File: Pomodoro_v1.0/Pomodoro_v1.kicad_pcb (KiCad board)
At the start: 2 copper layers, 70 x 50 mm, 88 parts, among them J1 BATT, J13 SWIM, J2 NTC, J3 USB_OTG, J5 UART, M1 MOUNTING-HOLE, M2 MOUNTING-HOLE, M3 MOUNTING-HOLE, M4 MOUNTING-HOLE, Q1 BC807, Q2 BC807, SW1 SLIDER, SW2 BUTTON_SPST, U1 MCP73833, U2 TPS62260, U3 STM8L151C2T6, U4 AS1122

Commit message: update footprints with 3D models
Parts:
- SW1: footprint SLIDE_SWITCHES: 5MS1S102AM6QE -> SLIDE_SWITCHES:5MS1S102AM6QE
- SW2: footprint NINIGI TACTS-24N-F:NINIGI TACTS-24N-F -> NINIGI_TACTS-24N-F:NINIGI_TACTS-24N-F
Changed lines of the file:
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@@
-(kicad_pcb (version 4) (host pcbnew 4.0.7-e2-6376~58~ubuntu16.04.1)
+(kicad_pcb (version 4) (host pcbnew 4.0.7)
   (general
     (links 166)
@@
     (pad_to_mask_clearance 0.2)
     (aux_axis_origin 0 0)
-    (visible_elements FFFEF77F)
+    (visible_elements 7FFFF7FF)
     (pcbplotparams
       (layerselection 0x00030_80000001)
@@
     (add_net VCC)
   )
-  (module BUZZERS_TDK:BUZZERS_TDK (layer F.Cu)
-    (at 60 102)
-    (fp_text reference BZ1 (at 0.254 -7.366) (layer F.SilkS)
-      (effects (font (size 1 1) (thickness 0.15)))
-    )
-    (fp_text value Buzzer (at 0 -2.286) (layer F.Fab)
-      (effects (font (size 1 1) (thickness 0.15)))
-    )
-    (fp_circle (center 0 0) (end 6.604 0) (layer F.SilkS) (width 0.15))
-    (pad 1 thru_hole circle (at 2.5 0) (size 2 2) (drill 0.8) (layers *.Cu *.Mask)
-      (net 1 VCC))
-    (pad 2 thru_hole circle (at -2.5 0) (size 2 2) (drill 0.8) (layers *.Cu *.Mask)
-      (net 2 /BUZZER))
-    (pad "" np_thru_hole circle (at 0 -4.5) (size 0.8 0.8) (drill 0.8) (layers *.Cu *.Mask))
-    (pad "" np_thru_hole circle (at 0 4.5) (size 0.8 0.8) (drill 0.8) (layers *.Cu *.Mask))
-  )
   (module Capacitors_SMD:C_0805 (layer F.Cu)
     (at 211.465001 119.155)
@@
     (pad 6 smd rect (at -2.9 0.35 270) (size 1.2 1.9) (layers F.Cu F.Mask)
       (net 4 GND))
-    (model ${KISYS3DMOD}/Connectors_USB.3dshapes/USB_Micro-B_Molex-105017-0001.wrl
+    (model ${KISYS3DMOD}/Connectors_USB.3dshapes/MOLEX_1050170001.wrl
       (at (xyz 0 0 0))
       (scale (xyz 1 1 1))
@@
     )
   )
-  (module "SLIDE_SWITCHES: 5MS1S102AM6QE" (layer F.Cu)
-    (at 40 79 270)
-    (fp_text reference SW1 (at -8.5 6 360) (layer F.SilkS)
-      (effects (font (size 1 1) (thickness 0.15)))
-    )
-    (fp_text value SLIDER (at -0.5 4 270) (layer F.Fab)
-      (effects (font (size 1 1) (thickness 0.15)))
-    )
-    (fp_line (start -0.5 11.5) (end -0.5 16) (layer F.SilkS) (width 0.15))
-    (fp_line (start -0.5 16) (end 3.5 16) (layer F.SilkS) (width 0.15))
-    (fp_line (start 3.5 16) (end 3.5 11.5) (layer F.SilkS) (width 0.15))
-    (fp_line (start 7.5 8) (end 7.5 2.5) (layer F.SilkS) (width 0.15))
-    (fp_line (start 7.5 2.5) (end -7.5 2.5) (layer F.SilkS) (width 0.15))
-    (fp_line (start -7.5 2.5) (end -7.5 8) (layer F.SilkS) (width 0.15))
-    (fp_line (start -7 11.5) (end 7.5 11.5) (layer F.SilkS) (width 0.15))
-    (pad 1 thru_hole circle (at 4.699 -0.127 270) (size 3 3) (drill 1.85) (layers *.Cu *.Mask)
-      (net 60 "Net-(SW1-Pad1)"))
-    (pad 2 thru_hole circle (at 0 0 270) (size 3 3) (drill 1.85) (layers *.Cu *.Mask)
-      (net 23 +BATT))
-    (pad 3 thru_hole circle (at -4.699 -0.127 270) (size 3 3) (drill 1.85) (layers *.Cu *.Mask)
-      (net 3 +4V))
-    (pad "" thru_hole circle (at 6.604 9.525 270) (size 3 3) (drill 1.85) (layers *.Cu *.Mask))
-    (pad "" thru_hole circle (at -6.604 9.525 270) (size 3 3) (drill 1.85) (layers *.Cu *.Mask))
-  )
-  (module "NINIGI TACTS-24N-F:NINIGI TACTS-24N-F" (layer F.Cu)
-    (at 39 99)
-    (fp_text reference SW2 (at 2 9.5) (layer F.SilkS)
-      (effects (font (size 1 1) (thickness 0.15)))
-    )
-    (fp_text value BUTTON_SPST (at 7 -4.5) (layer F.Fab)
-      (effects (font (size 1 1) (thickness 0.15)))
-    )
-    (fp_line (start 0 -1) (end 0 -3.5) (layer F.SilkS) (width 0.15))
-    (fp_line (start 0 8.5) (end 0 6) (layer F.SilkS) (width 0.15))
-    (fp_line (start 12 -3.5) (end 12 -1) (layer F.SilkS) (width 0.15))
-    (fp_line (start 12 5.5) (end 12 8.5) (layer F.SilkS) (width 0.15))
-    (fp_line (start 12 1) (end 12 4) (layer F.SilkS) (width 0.15))
-    (fp_line (start 0 8.5) (end 12 8.5) (layer F.SilkS) (width 0.15))
-    (fp_line (start 12 -3.5) (end 0 -3.5) (layer F.SilkS) (width 0.15))
-    (fp_line (start 0 1) (end 0 4) (layer F.SilkS) (width 0.15))
-    (pad 1 thru_hole rect (at 0 0) (size 2 2) (drill 1.2) (layers *.Cu *.Mask)
-      (net 56 /BUTTON))
-    (pad 2 thru_hole circle (at 12 0) (size 2 2) (drill 1.2) (layers *.Cu *.Mask)
-      (net 56 /BUTTON))
-    (pad 4 thru_hole circle (at 12 5) (size 2 2) (drill 1.2) (layers *.Cu *.Mask)
-      (net 4 GND))
-    (pad 3 thru_hole circle (at 0 5) (size 2 2) (drill 1.2) (layers *.Cu *.Mask)
-      (net 4 GND))
-  )
   (module Measurement_Points:Measurement_Point_Round-SMD-Pad_Small (layer F.Cu)
     (at 178.954762 136.995)
@@
       (at (xyz 0 0 0))
       (scale (xyz 1 1 1))
+      (rotate (xyz 0 0 0))
+    )
+  )
+  (module NINIGI_TACTS-24N-F:NINIGI_TACTS-24N-F (layer F.Cu)
+    (at 39 99)
+    (fp_text reference SW2 (at 2 9.5) (layer F.SilkS)
+      (effects (font (size 1 1) (thickness 0.15)))
+    )
+    (fp_text value BUTTON_SPST (at 7 -4.5) (layer F.Fab)
+      (effects (font (size 1 1) (thickness 0.15)))
+    )
+    (fp_line (start 0 -1) (end 0 -3.5) (layer F.SilkS) (width 0.15))
+    (fp_line (start 0 8.5) (end 0 6) (layer F.SilkS) (width 0.15))
+    (fp_line (start 12 -3.5) (end 12 -1) (layer F.SilkS) (width 0.15))
+    (fp_line (start 12 5.5) (end 12 8.5) (layer F.SilkS) (width 0.15))
+    (fp_line (start 12 1) (end 12 4) (layer F.SilkS) (width 0.15))
+    (fp_line (start 0 8.5) (end 12 8.5) (layer F.SilkS) (width 0.15))
+    (fp_line (start 12 -3.5) (end 0 -3.5) (layer F.SilkS) (width 0.15))
+    (fp_line (start 0 1) (end 0 4) (layer F.SilkS) (width 0.15))
+    (pad 1 thru_hole rect (at 0 0) (size 2 2) (drill 1.2) (layers *.Cu *.Mask)
+      (net 56 /BUTTON))
+    (pad 2 thru_hole circle (at 12 0) (size 2 2) (drill 1.2) (layers *.Cu *.Mask)
+      (net 56 /BUTTON))
+    (pad 4 thru_hole circle (at 12 5) (size 2 2) (drill 1.2) (layers *.Cu *.Mask)
+      (net 4 GND))
+    (pad 3 thru_hole circle (at 0 5) (size 2 2) (drill 1.2) (layers *.Cu *.Mask)
+      (net 4 GND))
+    (model E:/CURRENT/PROJECTS/POMODORO/Electronics/Libraries/WRL/NINIGI_TACTS_24N.wrl
+      (at (xyz 0 0 0))
+      (scale (xyz 1 1 1))
+      (rotate (xyz 0 0 0))
+    )
+  )
+  (module BUZZERS_TDK:BUZZERS_TDK (layer F.Cu)
+    (at 60 102)
+    (fp_text reference BZ1 (at 0.254 -7.366) (layer F.SilkS)
+      (effects (font (size 1 1) (thickness 0.15)))
+    )
+    (fp_text value Buzzer (at 0 -2.286) (layer F.Fab)
+      (effects (font (size 1 1) (thickness 0.15)))
+    )
+    (fp_circle (center 0 0) (end 6.604 0) (layer F.SilkS) (width 0.15))
+    (pad 1 thru_hole circle (at 2.5 0) (size 2 2) (drill 0.8) (layers *.Cu *.Mask)
+      (net 1 VCC))
+    (pad 2 thru_hole circle (at -2.5 0) (size 2 2) (drill 0.8) (layers *.Cu *.Mask)
+      (net 2 /BUZZER))
+    (pad "" np_thru_hole circle (at 0 -4.5) (size 0.8 0.8) (drill 0.8) (layers *.Cu *.Mask))
+    (pad "" np_thru_hole circle (at 0 4.5) (size 0.8 0.8) (drill 0.8) (layers *.Cu *.Mask))
+    (model E:/CURRENT/PROJECTS/POMODORO/Electronics/Libraries/WRL/BUZZER_TDK_PS12.wrl
+      (at (xyz 0 0 0))
+      (scale (xyz 1 1 1))
+      (rotate (xyz 0 0 0))
+    )
+  )
+  (module SLIDE_SWITCHES:5MS1S102AM6QE (layer F.Cu)
+    (at 40 79 270)
+    (fp_text reference SW1 (at -8.5 6 360) (layer F.SilkS)
+      (effects (font (size 1 1) (thickness 0.15)))
+    )
+    (fp_text value SLIDER (at -0.5 4 270) (layer F.Fab)
+      (effects (font (size 1 1) (thickness 0.15)))
+    )
+    (fp_line (start -0.5 11.5) (end -0.5 16) (layer F.SilkS) (width 0.15))
+    (fp_line (start -0.5 16) (end 3.5 16) (layer F.SilkS) (width 0.15))
+    (fp_line (start 3.5 16) (end 3.5 11.5) (layer F.SilkS) (width 0.15))
+    (fp_line (start 7.5 8) (end 7.5 2.5) (layer F.SilkS) (width 0.15))
+    (fp_line (start 7.5 2.5) (end -7.5 2.5) (layer F.SilkS) (width 0.15))
+    (fp_line (start -7.5 2.5) (end -7.5 8) (layer F.SilkS) (width 0.15))
+    (fp_line (start -7 11.5) (end 7.5 11.5) (layer F.SilkS) (width 0.15))
+    (pad 1 thru_hole circle (at 4.699 -0.127 270) (size 3 3) (drill 1.85) (layers *.Cu *.Mask)
+      (net 60 "Net-(SW1-Pad1)"))
+    (pad 2 thru_hole circle (at 0 0 270) (size 3 3) (drill 1.85) (layers *.Cu *.Mask)
+      (net 23 +BATT))
+    (pad 3 thru_hole circle (at -4.699 -0.127 270) (size 3 3) (drill 1.85) (layers *.Cu *.Mask)
+      (net 3 +4V))
+    (pad "" thru_hole circle (at 6.604 9.525 270) (size 3 3) (drill 1.85) (layers *.Cu *.Mask))
+    (pad "" thru_hole circle (at -6.604 9.525 270) (size 3 3) (drill 1.85) (layers *.Cu *.Mask))
+    (model E:/CURRENT/PROJECTS/POMODORO/Electronics/Libraries/WRL/5MS1S102AM6QE.wrl
+      (at (xyz 0 0 0))
+      (scale (xyz 1 1 1))

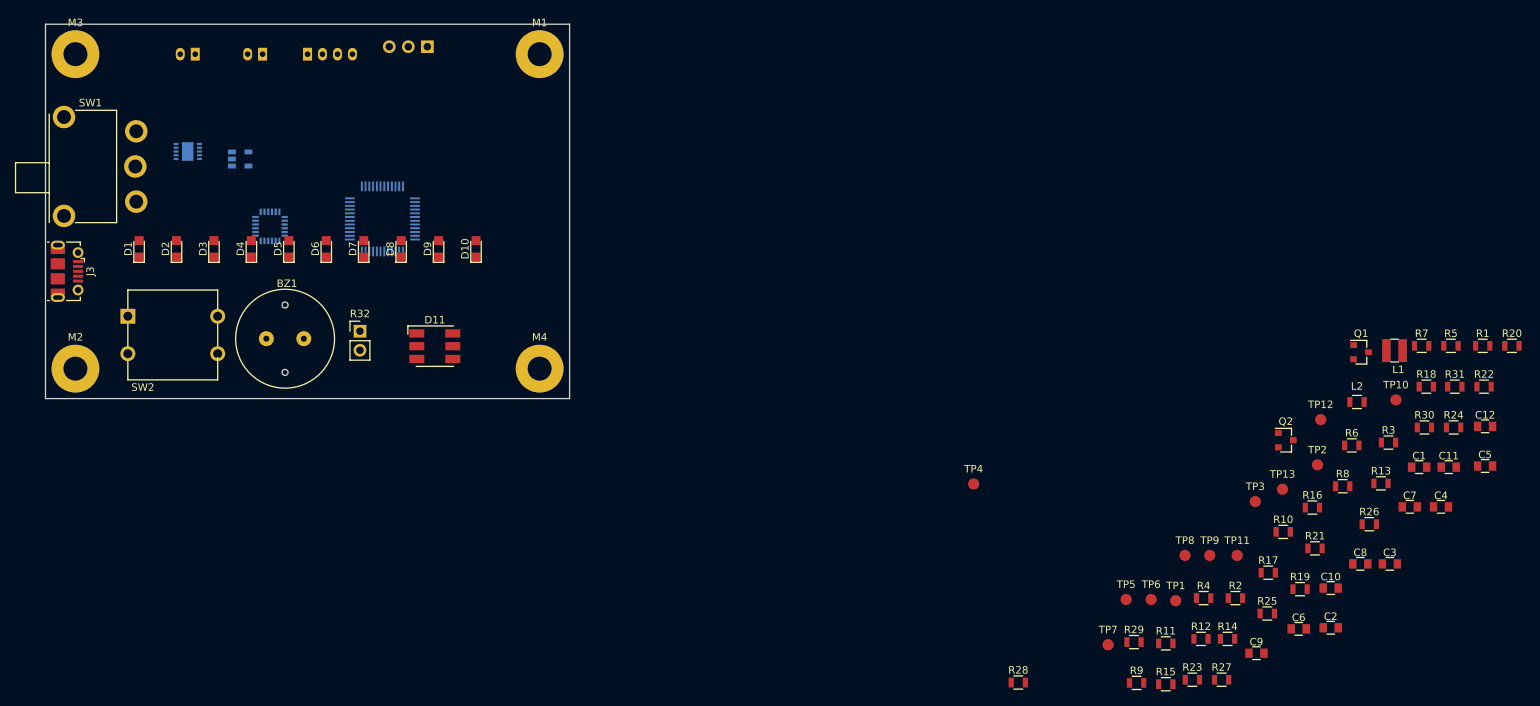
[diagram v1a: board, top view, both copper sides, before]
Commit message: Components placement done, initial routing (power tracks)
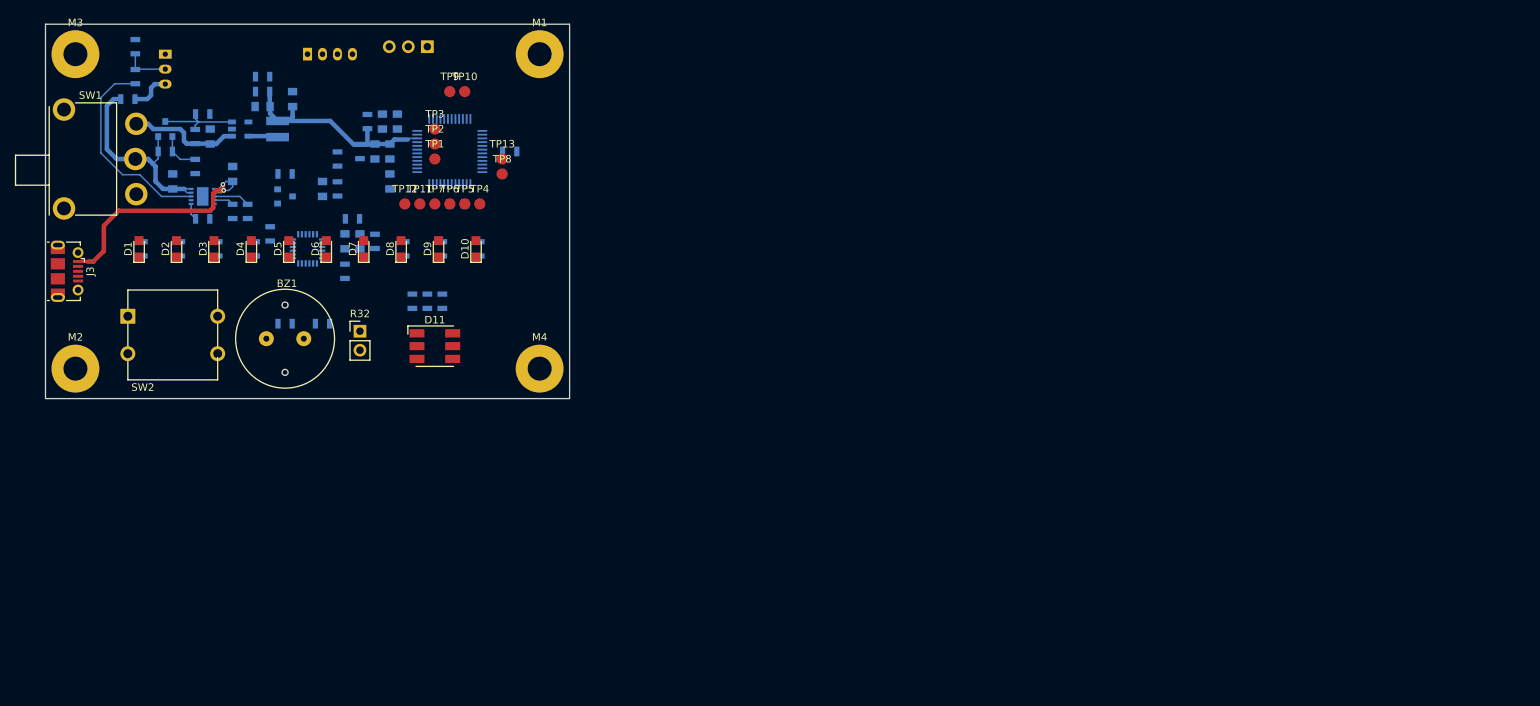
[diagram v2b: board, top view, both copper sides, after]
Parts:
- removed J2: NTC, Connectors_JST:JST_PH_S2B-PH-K_02x2.00mm_Angled
- added C13: 10u, Capacitors_SMD:C_0805, B.Cu at (53.0, 80.0)
- added C14: 10u, Capacitors_SMD:C_0805, B.Cu at (45.0, 81.0)
- added R33: 0R, Resistors_SMD:R_0805, B.Cu at (39.0, 70.0)
- added R34: 10K, Resistors_SMD:R_0805, B.Cu at (48.0, 75.0)
- C1, C10, C11, C12, C2, C3, C4, C5, C6, C7, C8, C9, L1, L2, Q1, Q2, R1, R10, R11, R12, R13, R14, R15, R16, R17, R18, R19, R2, R20, R21, R22, R23, R24, R25, R26, R27, R28, R29, R3, R30, R31, R4, R5, R6, R7, R8, R9: moved to B.Cu
- J1: footprint Connectors_JST:JST_PH_S2B-PH-K_02x2.00mm_Angled -> Connectors_JST:s3b-ph-kl
- moved R20 187.3 mm to (40.0, 67.0), turned to 90 degrees
- moved R1 179.4 mm to (41.0, 90.0), turned to 90 degrees
- moved R18 178.3 mm to (40.0, 63.0), turned to 90 degrees
- moved R5 169.4 mm to (48.0, 79.0), turned to 270 degrees
- moved R22 168.3 mm to (57.0, 67.0)
- moved C1 167.4 mm to (50.0, 75.0), turned to 90 degrees
- moved R24 163.6 mm to (55.0, 85.0), turned to 90 degrees
- moved R8 163.5 mm to (44.0, 77.0)
- moved Q1 162.5 mm to (44.0, 74.0), turned to 90 degrees
- moved C5 159.6 mm to (65.0, 82.0), turned to 270 degrees
- moved C3 159.2 mm to (61.0, 70.0), turned to 90 degrees
- moved C2 158.7 mm to (57.0, 71.0), turned to 180 degrees
- moved R3 158.5 mm to (51.0, 90.0), turned to 90 degrees
- moved R10 154.7 mm to (49.0, 72.0)
- moved R19 154.7 mm to (49.0, 86.0)
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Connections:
- J1 pad 2: +BATT -> Net-(J1-Pad2)
- Q1 pad 3: +4V -> Net-(Q1-Pad3)
- R10 pad 1: +4V -> Net-(Q1-Pad3)
- R18 pad 1: Net-(J2-Pad2) -> Net-(J1-Pad2)
- R20 pad 2: Net-(J2-Pad2) -> Net-(J1-Pad2)
- U2 pad 3: +4V -> Net-(Q1-Pad3)
- U4 pad 14: /AS_RST -> /AS_IRQ
- U4 pad 15: (no net) -> /AS_RST
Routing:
- net VBUS: track 0.00 -> 33.8 mm, vias 0 -> 2
- net VCC: track 0.00 -> 30.4 mm
- net +BATT: track 0.00 -> 29.0 mm
- net /THERM: track 0.00 -> 27.2 mm
- net +4V: track 0.00 -> 15.0 mm
- net Net-(Q1-Pad3): track 0.00 -> 11.5 mm
- net Net-(J1-Pad2): track 0.00 -> 6.12 mm
- net Net-(Q1-Pad1): track 0.00 -> 5.48 mm
- net Net-(J1-Pad3): track 0.00 -> 5.46 mm
- net /STAT1: track 0.00 -> 4.88 mm
- net Net-(L1-Pad1): track 0.00 -> 3.95 mm
- net /STAT2: track 0.00 -> 2.68 mm
- net Net-(R19-Pad1): track 0.00 -> 2.25 mm
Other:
- net class Default: trace_width 0.25 -> 0.2; via_drill 0.4 -> 0.3
- rule via_min_size: 0.4 -> 0.6

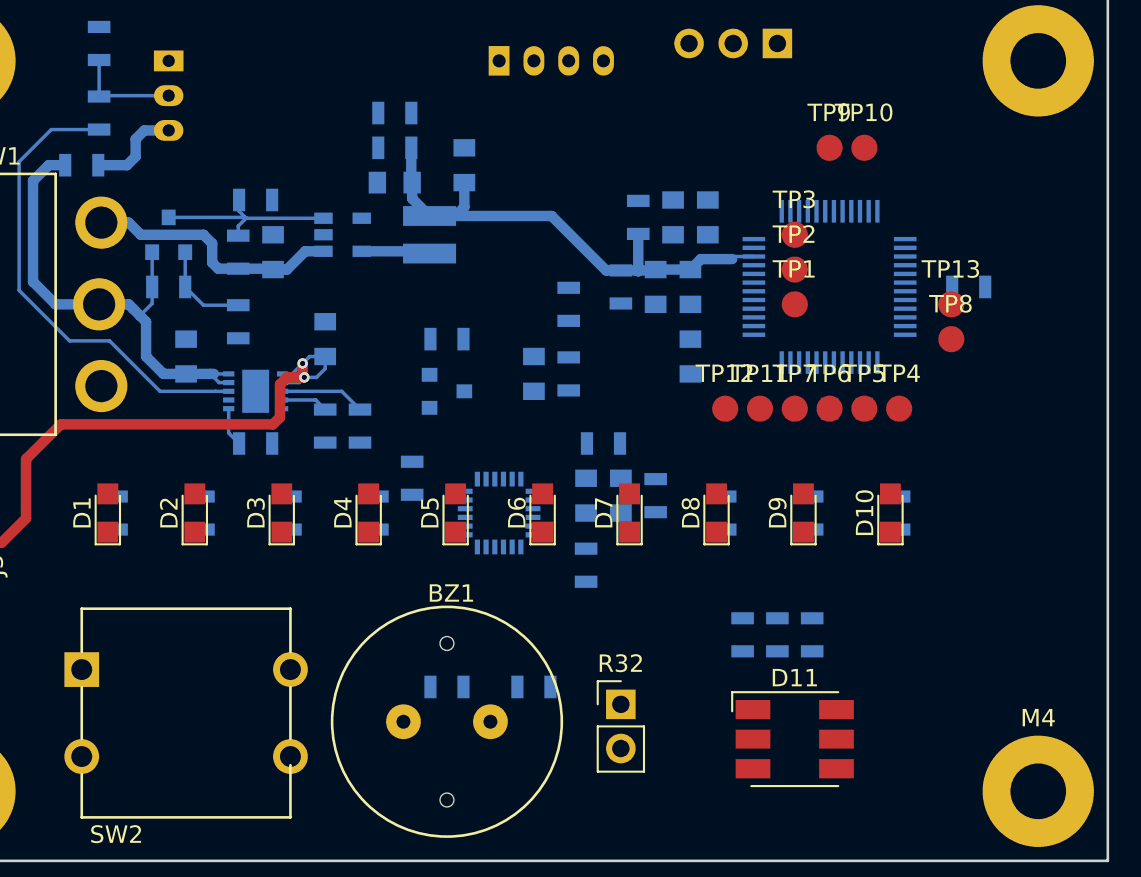
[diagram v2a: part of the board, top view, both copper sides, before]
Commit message: routing in progress (mainly CPU section)
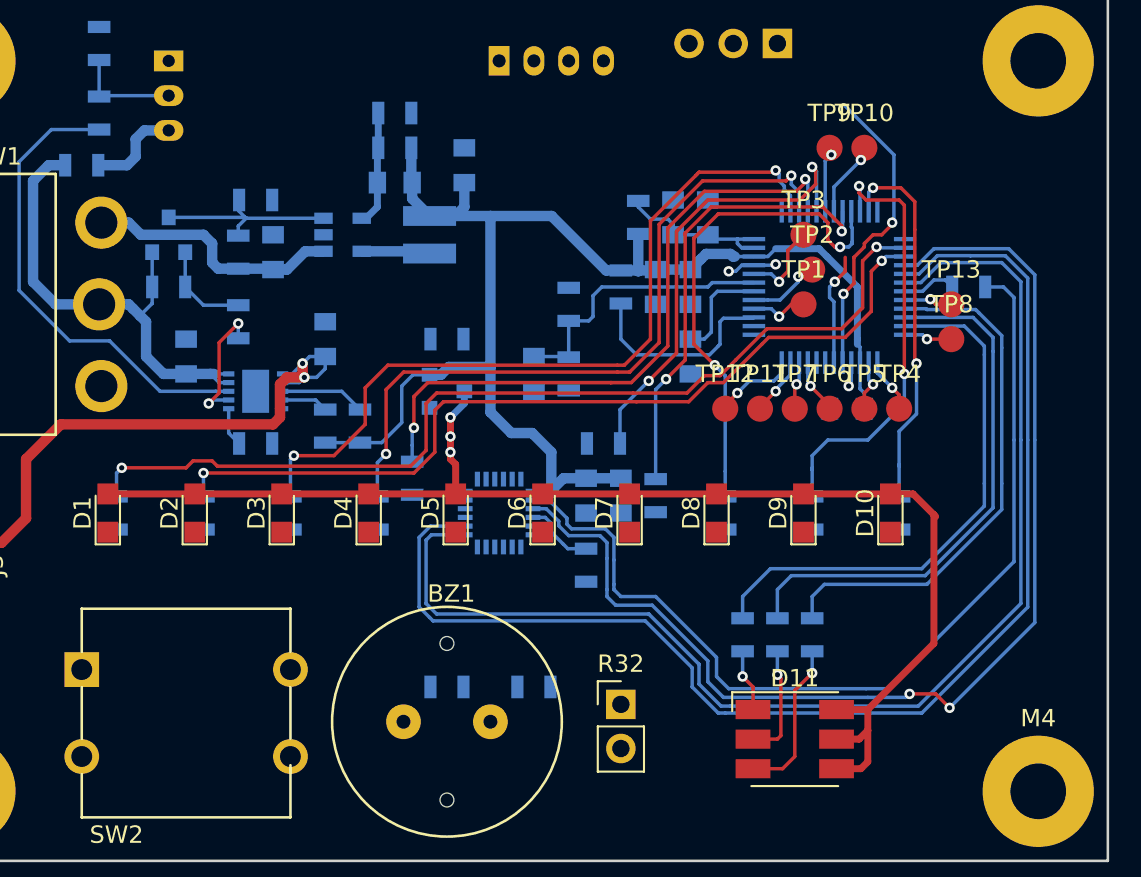
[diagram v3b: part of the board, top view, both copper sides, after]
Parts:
- moved TP2 1.00 mm to (81.0, 76.0)
- moved TP1 0.50 mm to (80.5, 78.0)
- moved TP3 0.50 mm to (80.5, 74.0)
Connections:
- U3 pad 43: /STAT_1 -> /STAT1
- U3 pad 44: /STAT_2 -> /STAT2
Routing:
- net Net-(D1-Pad2): track 0.00 -> 76.0 mm, vias 0 -> 3
- net /AS_CLK: track 0.00 -> 74.5 mm
- net /AS_SD: track 0.00 -> 71.9 mm
- net /AS_RST: track 0.00 -> 66.9 mm, vias 0 -> 2
- net /PWM_R1: track 0.00 -> 55.5 mm, vias 0 -> 2
- net /AS_IRQ: track 0.00 -> 54.9 mm
- net VCC: track 30.4 -> 80.4 mm
- net /PWM_R2: track 0.00 -> 49.6 mm, vias 0 -> 2
- net /PWM_Y1: track 0.00 -> 44.8 mm, vias 0 -> 2
- net /PWM_Y2: track 0.00 -> 41.0 mm, vias 0 -> 2
- net /PWM_Y3: track 0.00 -> 37.6 mm, vias 0 -> 2
- net /PWM_RGB_B: track 0.00 -> 31.5 mm
- net /PWM_RGB_G: track 0.00 -> 31.3 mm
- net /PWM_RGB_R: track 0.00 -> 30.4 mm
- net /PWM_G2: track 0.00 -> 28.6 mm, vias 0 -> 2
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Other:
- net class Default: clearance 0.2 -> 0.195
- rule trace_clearance: 0.2 -> 0.195
